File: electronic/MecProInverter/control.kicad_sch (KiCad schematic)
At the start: 54 parts, among them J1 0022232031, J2 0022232031, J5 Conn_01x08, J6 LM61, J7 Conn_01x11, Q1 DMN3404L, SW1 PTS645SM95SMTR92LFS, SW2 PTS645SM95SMTR92LFS, SW3 PTS645SM95SMTR92LFS, U1 ESP32-S3-MINI-1-N8, U2 ADUM3160, U3 TYPE-C_16PIN_2MD(073), U6 SKRKAEE020, U7 SKRKAEE020

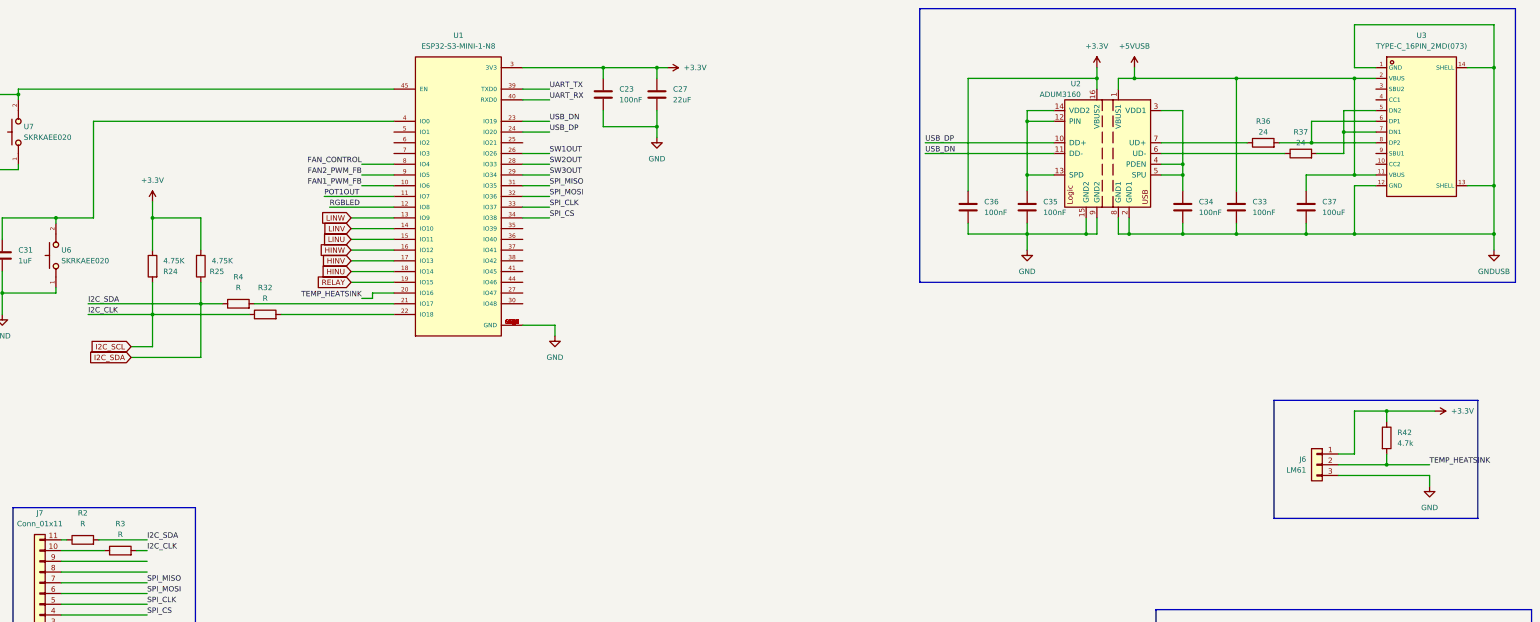
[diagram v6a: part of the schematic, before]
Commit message: Electronic
Currentsensor updated
Power structure updated
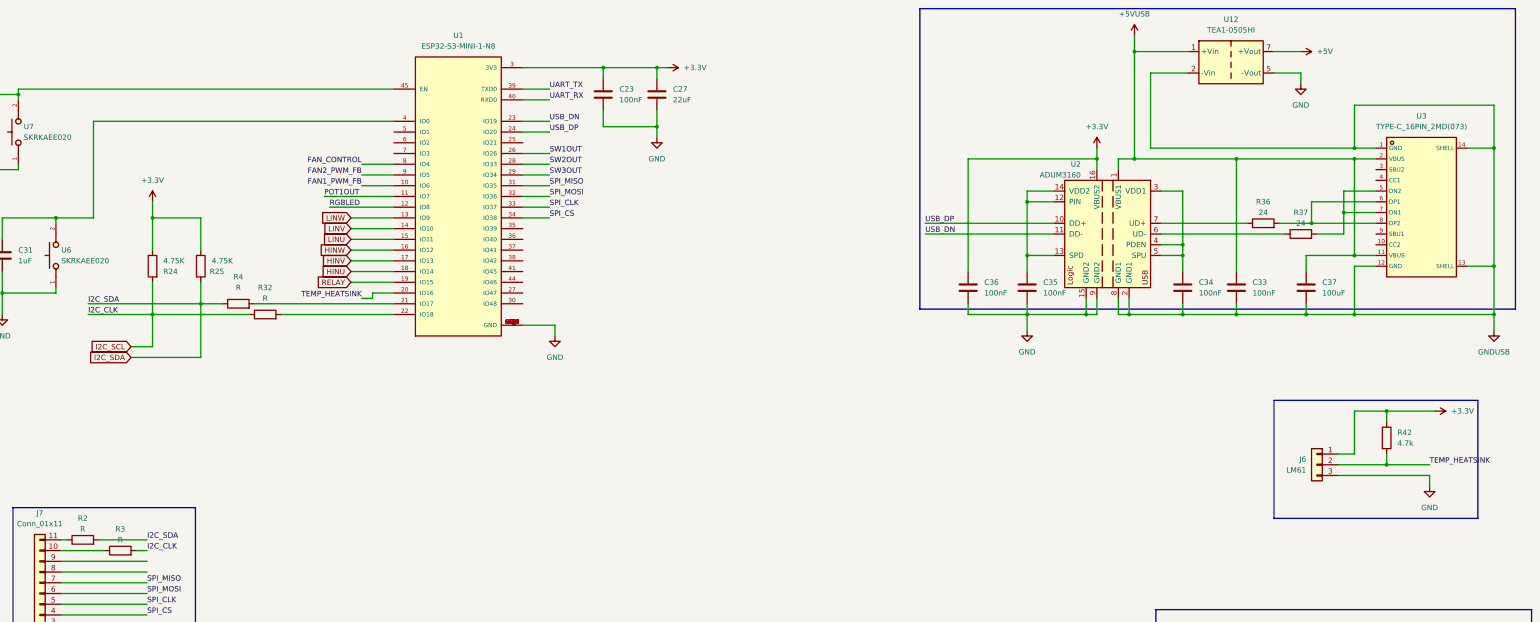
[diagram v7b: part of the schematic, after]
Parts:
- added U12: TEA1-0505HI, Converter_DCDC:Converter_DCDC_TRACO_TEA1HI-xxxx_THT, symbol Converter_DCDC:TEA1-0505HI
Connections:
- net +5V: now also U12.1 (+Vin), U12.7 (+Vout)
- net GND: now also U12.2 (-Vin), U12.5 (-Vout)
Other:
- moved on the sheet: C33, C34, C35, C36, C37, R36, R37, U2, U3

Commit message: Electronic
Rework: Fan, ESP32 Pinout, 15V Power,
Added: GPIO ISO, ESD
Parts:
- added C46, C47, C48, C49: 100nF, symbol Device:C
- added C50: 1uF, symbol Device:C
- added J3: Screw_Terminal_01x06, symbol Connector:Screw_Terminal_01x06
- added R49, R50, R51, R52: 180, symbol Device:R
- added R53, R54, R55, R56: R, symbol Device:R
- added R57, R58, R59: 10k, symbol Device:R
- added TP1, TP2, TP3, TP4: TestPoint, Connector_Pin:Pin_D1.0mm_L10.0mm_LooseFit, symbol Connector:TestPoint
- added TP5: MTCK, Connector_Pin:Pin_D1.0mm_L10.0mm_LooseFit, symbol Connector:TestPoint
- added TP6: MTDO, Connector_Pin:Pin_D1.0mm_L10.0mm_LooseFit, symbol Connector:TestPoint
- added TP7: MTMS, Connector_Pin:Pin_D1.0mm_L10.0mm_LooseFit, symbol Connector:TestPoint
- added TP8: MTDI, Connector_Pin:Pin_D1.0mm_L10.0mm_LooseFit, symbol Connector:TestPoint
- added U14, U17: PSRV05-4MR6T1G, footprint:SOT-23-6_L2.9-W1.6-P0.95-LS2.8-BL, symbol PSRV05-4MR6T1G:PSRV05-4MR6T1G
- added U15, U16: ADUM1201ARZ-RL7, footprint:SOIC-8_L4.9-W3.9-P1.27-LS6.0-BL, symbol ADUM1201ARZ-RL7:ADUM1201ARZ-RL7
- added U18: PMV100EPAR, footprint:SOT-23-3_L2.9-W1.3-P1.90-LS2.3-BR, symbol PMV100EPAR:PMV100EPAR
- R19: value 100k -> 10k
- R2, R3, R32, R4: value R -> 121
- R23: value 100K -> 10k
- R24, R25: value 4.75K -> 1.6k
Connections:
- net +15V: now also C32.1, R57.1, U18.2 (S); no longer R31.1
- net +3.3V: now also C47.1, C48.1, R58.1, R59.1, U15.1 (VDD1), U16.1 (VDD1)
- net +5V: no longer C33.1, C37.1, U12.1 (+Vin), U2.1 (VBUS1), U3.11 (VBUS), U3.2 (VBUS)
- net FAN1_PWM_FB: now also U1.6 (IO2), R58.2; no longer U1.10 (IO6)
- net FAN2_PWM_FB: now also U1.7 (IO3), R59.2; no longer U1.9 (IO5)
- net FAN_CONTROL: now also U1.5 (IO1); no longer U1.8 (IO4)
- net GND: now also D5.2 (A), J1.1, J2.1, C47.2, C48.2, C50.2, U15.4 (GND1), U16.4 (GND1); no longer C33.2, C34.2, C37.2, U12.2 (-Vin), U2.2 (GND1), U2.8 (GND1), U3.1 (GND), U3.12 (GND), U3.13 (SHELL), U3.14 (SHELL)
- net HINU: now also U1.19 (IO15); no longer U1.18 (IO14)
- net HINV: now also U1.18 (IO14); no longer U1.17 (IO13)
- net HINW: now also U1.17 (IO13); no longer U1.16 (IO12)
- net LINU: now also U1.16 (IO12); no longer U1.15 (IO11)
- net LINV: now also U1.15 (IO11); no longer U1.14 (IO10)
- net LINW: now also U1.14 (IO10); no longer U1.13 (IO9)
- net POT1OUT: now also U1.8 (IO4), C50.1; no longer U1.11 (IO7)
- net RELAY: now also U1.20 (IO16); no longer U1.19 (IO15)
- net RGBLED: now also U1.21 (IO17); no longer U1.12 (IO8)
- net SPI_CLK: now also U1.32 (IO36); no longer U1.33 (IO37)
- net SPI_CS: now also U1.29 (IO34); no longer U1.34 (IO38)
- net SPI_MISO: now also U1.33 (IO37); no longer U1.31 (IO35)
- net SPI_MOSI: now also U1.31 (IO35); no longer U1.32 (IO36)
- net SW1OUT: now also U1.9 (IO5); no longer U1.26 (IO26)
- net SW2OUT: now also U1.10 (IO6); no longer U1.28 (IO33)
- net SW3OUT: now also U1.11 (IO7); no longer U1.29 (IO34)
- net TEMP_HEATSINK: now also U1.22 (IO18); no longer U1.20 (IO16)
- net UART_RX: now also J7.9 (Pin_9), U16.2 (VOA)
- net UART_TX: now also J7.8 (Pin_8), U16.3 (VIB)
- net at R37.1, U2.6 (UD-): now also U14.6
- net at R36.1, U2.7 (UD+): now also U14.4
- net at D5.1 (K), J1.2, J2.2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: no longer C32.1
- net at R4.2: now also U1.12 (IO8); no longer U1.21 (IO17)
- net at R32.2: now also U1.13 (IO9); no longer U1.22 (IO18)
- net ISO_GPIO_1: now reaches U1.25 (IO21)
- net ISO_GPIO_1: now also U15.2 (VOA)
- net at U1.35 (IO39): now also TP5.1
- net at U1.36 (IO40): now also TP6.1
- net at U1.37 (IO41): now also TP8.1
- net at U1.38 (IO42): now also TP7.1
- net at J5.3 (Pin_3): now also R53.1
- net at J5.4 (Pin_4): now also R54.1
- net at J5.5 (Pin_5): now also R55.1
- net at J5.6 (Pin_6): now also R56.1
- new net: Q1.3 (D), R57.2, U18.1 (G)
- new net: R50.1, U15.6 (VOB), U17.6
- new net: J3.2 (Pin_2), R50.2
- new net: R53.2, TP1.1
- new net: R52.1, U16.6 (VOB), U17.1
- new net: J3.4 (Pin_4), R52.2
- new net: R55.2, TP3.1
- new net: R56.2, TP4.1
- new net: R54.2, TP2.1
- new net: R51.1, U16.7 (VIA), U17.3
- new net: J3.3 (Pin_3), R51.2
- new net: R31.1, U18.3 (D)
- new net: R49.2, U15.7 (VIA), U17.4
- new net: J3.1 (Pin_1), R49.1
- new net +5VD: C33.1, C37.1, U12.1 (+Vin), U14.5, U2.1 (VBUS1), U3.11 (VBUS), U3.2 (VBUS)
- new net GNDD: C33.2, C34.2, C37.2, U12.2 (-Vin), U14.2, U2.2 (GND1), U2.8 (GND1), U3.1 (GND), U3.12 (GND), U3.13 (SHELL), U3.14 (SHELL)
- new net GNDS: C46.2, C49.2, J3.6 (Pin_6), U15.5 (GND2), U16.5 (GND2), U17.2
- new net ISO_GPIO_2: U1.34 (IO38), U15.3 (VIB)
- new net VSS: C46.1, C49.1, J3.5 (Pin_5), U15.8 (VDD2), U16.8 (VDD2), U17.5
- no-connect marks 5 -> 8
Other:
- moved on the sheet: C23, C27, C28, C29, C30, C31, C33, C34, C35, C36, C37, C5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
